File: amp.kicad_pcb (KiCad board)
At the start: 2 copper layers, 36 x 14 mm, 26 parts, among them IC1 STM32F103CBU6, IC2 MCP1700, J1 SERIAL, J2 MICROUSB, P1 SWD_TC, P2 SWD, Q1 FDV304P, Y1 8MHz

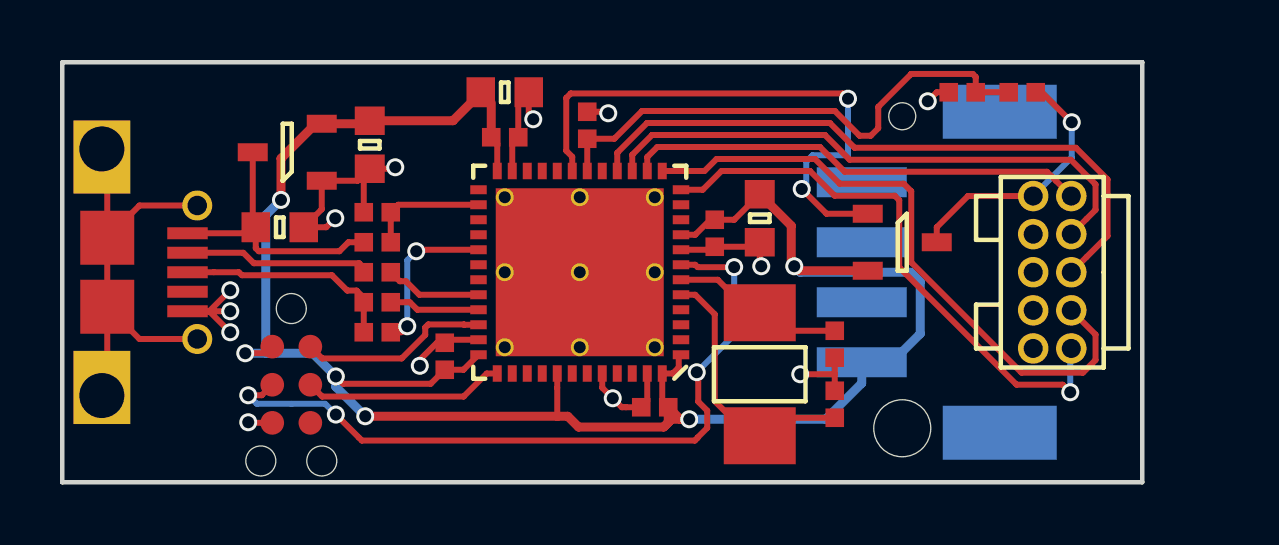
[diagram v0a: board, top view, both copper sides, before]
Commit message: fully routed
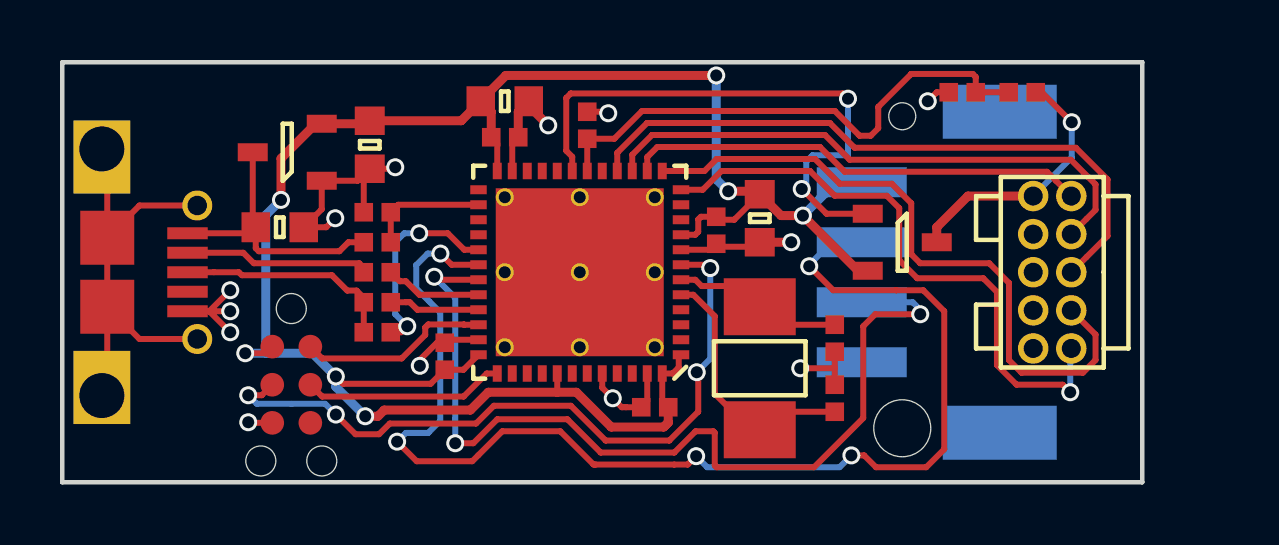
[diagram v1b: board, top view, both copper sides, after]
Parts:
- moved C1 0.30 mm to (113.2, 94.3)
- moved C7 0.20 mm to (124.2, 104.2)
- moved C9 0.20 mm to (124.2, 102.2)
- moved Y1 0.20 mm to (121.8, 103.2)
- moved C6 0.11 mm to (120.3, 98.6)
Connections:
- J1 pad 1: GND -> VDD
- J1 pad 2: /RXD -> /TXD
- J1 pad 3: /TXD -> /RXD
- J1 pad 4: VDD -> GND
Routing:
- net /TXD: track 0.00 -> 41.7 mm, vias 0 -> 5
- net /RXD: track 0.00 -> 31.2 mm, vias 0 -> 3
- net VDD: track 68.8 -> 66.7 mm, vias 6 -> 7
- net Net-(IC1-Pad29): track 5.35 -> 6.73 mm
- net GND: track 28.9 -> 30.2 mm
- net /RST: track 19.1 -> 20.2 mm
- net /TDI: track 21.2 -> 22.4 mm
- net /NRST: track 24.9 -> 23.8 mm

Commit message: silk etc
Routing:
- net Net-(C8-Pad2): track 17.7 -> 16.7 mm
- net /TXD: track 41.7 -> 40.9 mm
- net VDD: track 66.7 -> 67.4 mm
- net /RXD: track 31.2 -> 30.5 mm
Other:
- board text added: "+"
- board text added: "-"
- board text added: "AMP r1 2016-01-01"
- board text added: "Adam Magic Probe r1 github.com/adamgreig/amp"
- board text added: "R"
- board text added: "T"

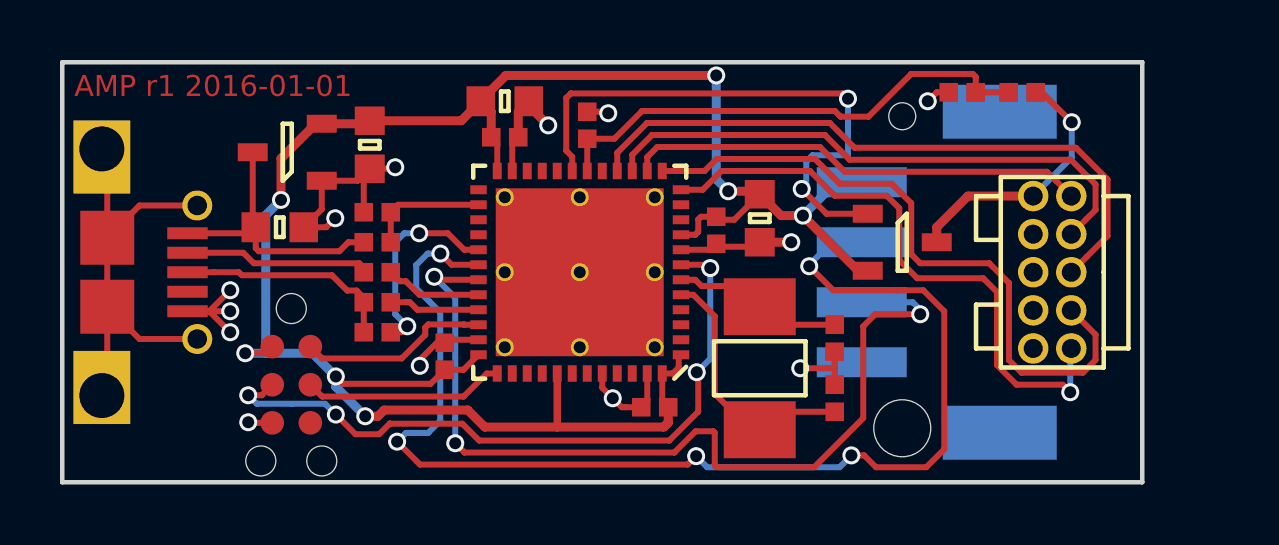
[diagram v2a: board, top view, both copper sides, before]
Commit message: try swap to surface-mount swd connector
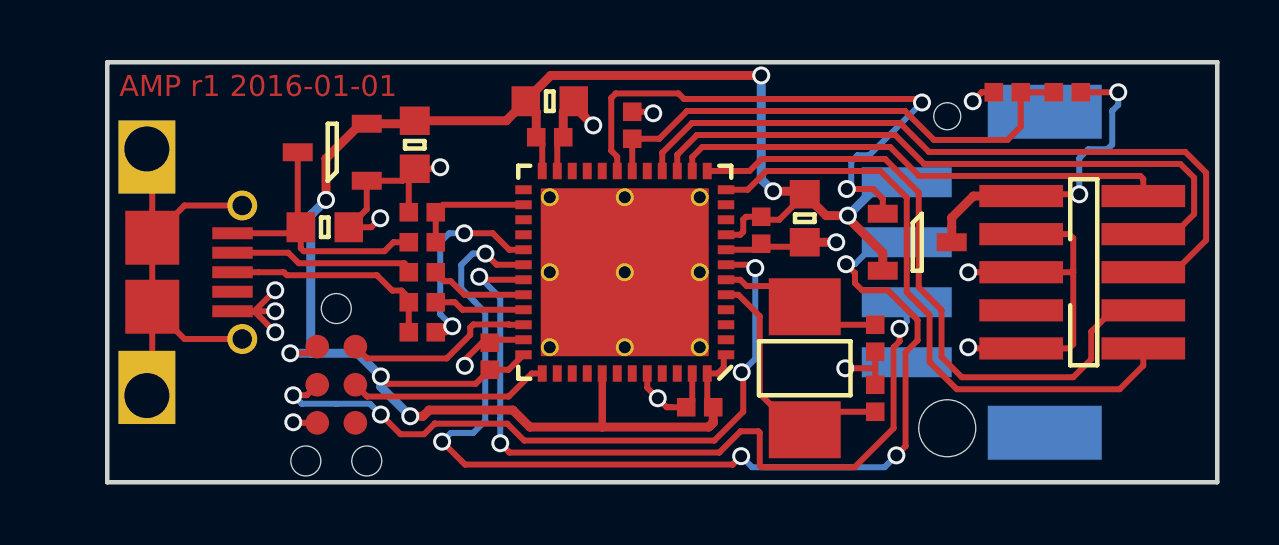
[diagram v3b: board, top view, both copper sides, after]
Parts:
- P2: footprint agg:FTSH-105-01-F-D-K -> agg:FTSH-105-01-L-DV-K
- moved C1 1.50 mm to (114.8, 94.3)
- moved C10 1.50 mm to (107.2, 98.5)
- moved C11 1.50 mm to (110.2, 95.8)
- moved C2 1.50 mm to (123.2, 98.2)
- moved C3 1.50 mm to (114.8, 95.5)
- moved C4 1.50 mm to (119.8, 104.5)
- moved C5 1.50 mm to (112.8, 102.8)
- moved C6 1.50 mm to (121.8, 98.6)
- moved C8 1.50 mm to (117.5, 95.1)
- moved IC1 1.50 mm to (117.2, 100.0)
- moved IC2 1.50 mm to (107.5, 96.0)
- moved J1 1.50 mm to (128.0, 100.0)
- moved J2 1.50 mm to (101.5, 100.0)
- moved P1 1.50 mm to (107.6, 103.8)
- moved R1 1.50 mm to (110.5, 99.0)
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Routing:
- net GND: track 30.2 -> 42.4 mm, vias 13 -> 15
- net /TXD: track 40.9 -> 36.0 mm
- net /RXD: track 30.5 -> 26.9 mm
- net /TDO: track 21.7 -> 24.6 mm
- net /TCK: track 18.9 -> 21.8 mm
- net /TPWR: track 8.75 -> 11.2 mm, vias 1 -> 2
- net /TMS: track 15.4 -> 16.6 mm
- net VDD: track 67.4 -> 66.7 mm
- net /RST: track 20.2 -> 20.8 mm, vias 1 -> 0
- net Net-(C8-Pad2): track 16.7 -> 17.2 mm
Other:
- board size 36 x 14 mm -> 37 x 14 mm

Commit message: ok, render gerbers for panel
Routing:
- net Net-(J2-PadS): track 15.3 -> 0.00 mm
- net GND: track 42.4 -> 40.5 mm, vias 15 -> 17
- net /TXD: track 36.0 -> 37.2 mm
- net VDD: track 66.7 -> 67.7 mm
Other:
- outline, holes or cut-outs redrawn

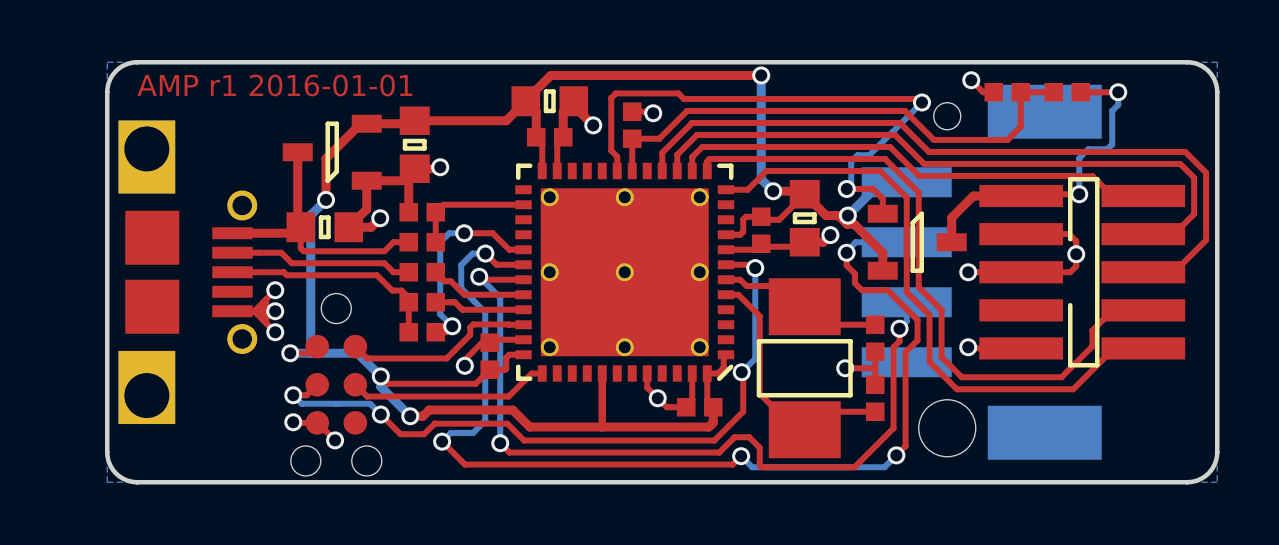
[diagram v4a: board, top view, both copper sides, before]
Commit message: redo panel with new usb and jst connectors
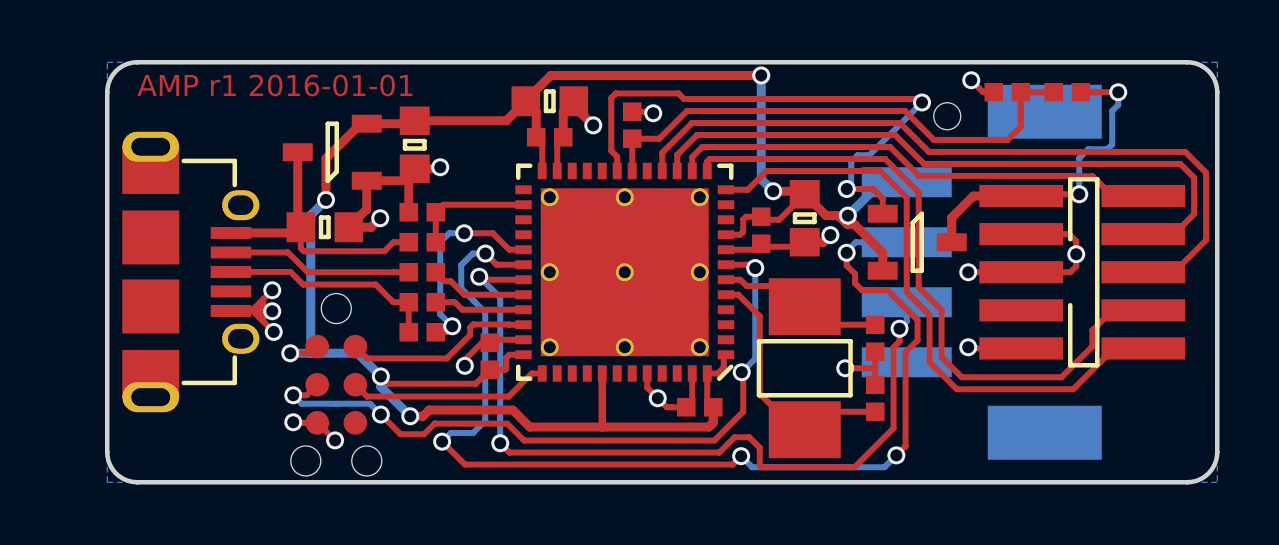
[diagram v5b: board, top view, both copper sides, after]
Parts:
- moved J2 0.05 mm to (101.5, 100.0), turned to 270 degrees
